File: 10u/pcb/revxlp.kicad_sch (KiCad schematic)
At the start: 126 parts, among them Q1 AO3416 N-channel MOSFET, SW1 SW_SPDT, SW2 SW_Push, U1 74HC595, U2 SeeeduinoXIAO_BLE

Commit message: feat: Optional backlighting for the bottom side.
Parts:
- added D_U0, D_U1, D_U10, D_U11, D_U2, D_U3, D_U4, D_U5, D_U6, D_U7, D_U8, D_U9: LED, Diode_SMD:D_1206_3216Metric_Pad1.42x1.75mm_HandSolder, symbol Device:LED
- added JP2: SolderJumper_2_Open, Jumper:SolderJumper-2_P1.3mm_Open_RoundedPad1.0x1.5mm, symbol Jumper:SolderJumper_2_Open
- added JP3: SolderJumper_2_Bridged, Jumper:SolderJumper-2_P1.3mm_Bridged_RoundedPad1.0x1.5mm, symbol Jumper:SolderJumper_2_Bridged
- added R_U0, R_U1, R_U10, R_U11, R_U2, R_U3, R_U4, R_U5, R_U6, R_U7, R_U8, R_U9: R, Resistor_SMD:R_1206_3216Metric_Pad1.30x1.75mm_HandSolder, symbol Device:R_Small_US
- JP1: footprint Jumper:SolderJumper-3_P1.3mm_Open_RoundedPad1.0x1.5mm -> Jumper:SolderJumper-3_P1.3mm_Bridged12_RoundedPad1.0x1.5mm; symbol 41_1350_pcb-rescue:SolderJumper_3_Open-Jumper -> Jumper:SolderJumper_3_Bridged12
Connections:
- net +3V3: now also JP1.3 (B); no longer JP1.1 (A)
- net +5V: now also D_U0.2 (A), D_U1.2 (A), D_U10.2 (A), D_U11.2 (A), D_U2.2 (A), D_U3.2 (A), D_U4.2 (A), D_U5.2 (A), D_U6.2 (A), D_U7.2 (A), D_U8.2 (A), D_U9.2 (A)
- net ledOut: now also JP3.1 (A); no longer Q1.3 (D)
- net at U2.14 (5V): now also JP1.1 (A); no longer JP1.3 (B)
- new net: JP2.2 (B), JP3.2 (B), Q1.3 (D)
- new net: D_U9.1 (K), R_U9.2
- new net: D_U11.1 (K), R_U11.2
- new net: D_U2.1 (K), R_U2.2
- new net: D_U3.1 (K), R_U3.2
- new net: D_U4.1 (K), R_U4.2
- new net: D_U10.1 (K), R_U10.2
- new net: D_U1.1 (K), R_U1.2
- new net: D_U8.1 (K), R_U8.2
- new net: D_U6.1 (K), R_U6.2
- new net: D_U5.1 (K), R_U5.2
- new net: D_U0.1 (K), R_U0.2
- new net: D_U7.1 (K), R_U7.2
- new net ledBottomOut: JP2.1 (A), R_U0.1, R_U1.1, R_U10.1, R_U11.1, R_U2.1, R_U3.1, R_U4.1, R_U5.1, R_U6.1, R_U7.1, R_U8.1, R_U9.1

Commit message: PCBA tweaks for 10u version.
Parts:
- BT2: MPN (none) -> SM02B-SRSS-TB(LF)(SN)
- D_A1: value D -> 1N4148W; MPN (none) -> 1N4148W
- D_A2, D_A3, D_A4, D_A5, D_B1, D_B2, D_B3, D_B4, D_B5, D_C1, D_C2, D_C3, D_C4, D_C5, D_D1, D_D2, D_D3, D_D4, D_D5, D_E1, D_E2, D_E3, D_E4, D_E5, D_F1, D_F2, D_F3, D_F4, D_F5, D_G0, D_G1, D_G2, D_G3, D_G4, D_G5: value D -> 1N4148W
- D_U0, D_U1: MPN (none) -> VLMB41P1Q2
- H1, H2, H3, H4, H5, H6, H7: MPN (none) -> SMTSO2020CTJ
- Q1: MPN (none) -> AO3416
- R_A1, R_A2, R_A3, R_A4, R_A5, R_AltG2, R_B1, R_B2, R_B3, R_B4, R_B5, R_C1, R_C2, R_C3, R_C4, R_C5, R_D1, R_D2, R_D3, R_D4, R_D5, R_E1, R_E2, R_E3, R_E4, R_E5, R_F1, R_F2, R_F3, R_F4, R_F5, R_G0, R_G1, R_G2, R_G3, R_G4, R_G5, R_U0, R_U1, R_U10, R_U11, R_U2, R_U3, R_U4, R_U5, R_U6, R_U7, R_U8, R_U9: value R -> 180
- SW1: MPN (none) -> PCM12
- SW2: MPN (none) -> EVQPUC02K
- SwA1, SwA2: MPN (none) -> CPG135001S30,VLMB41P1Q2
- U1: MPN (none) -> SN74HC595DR

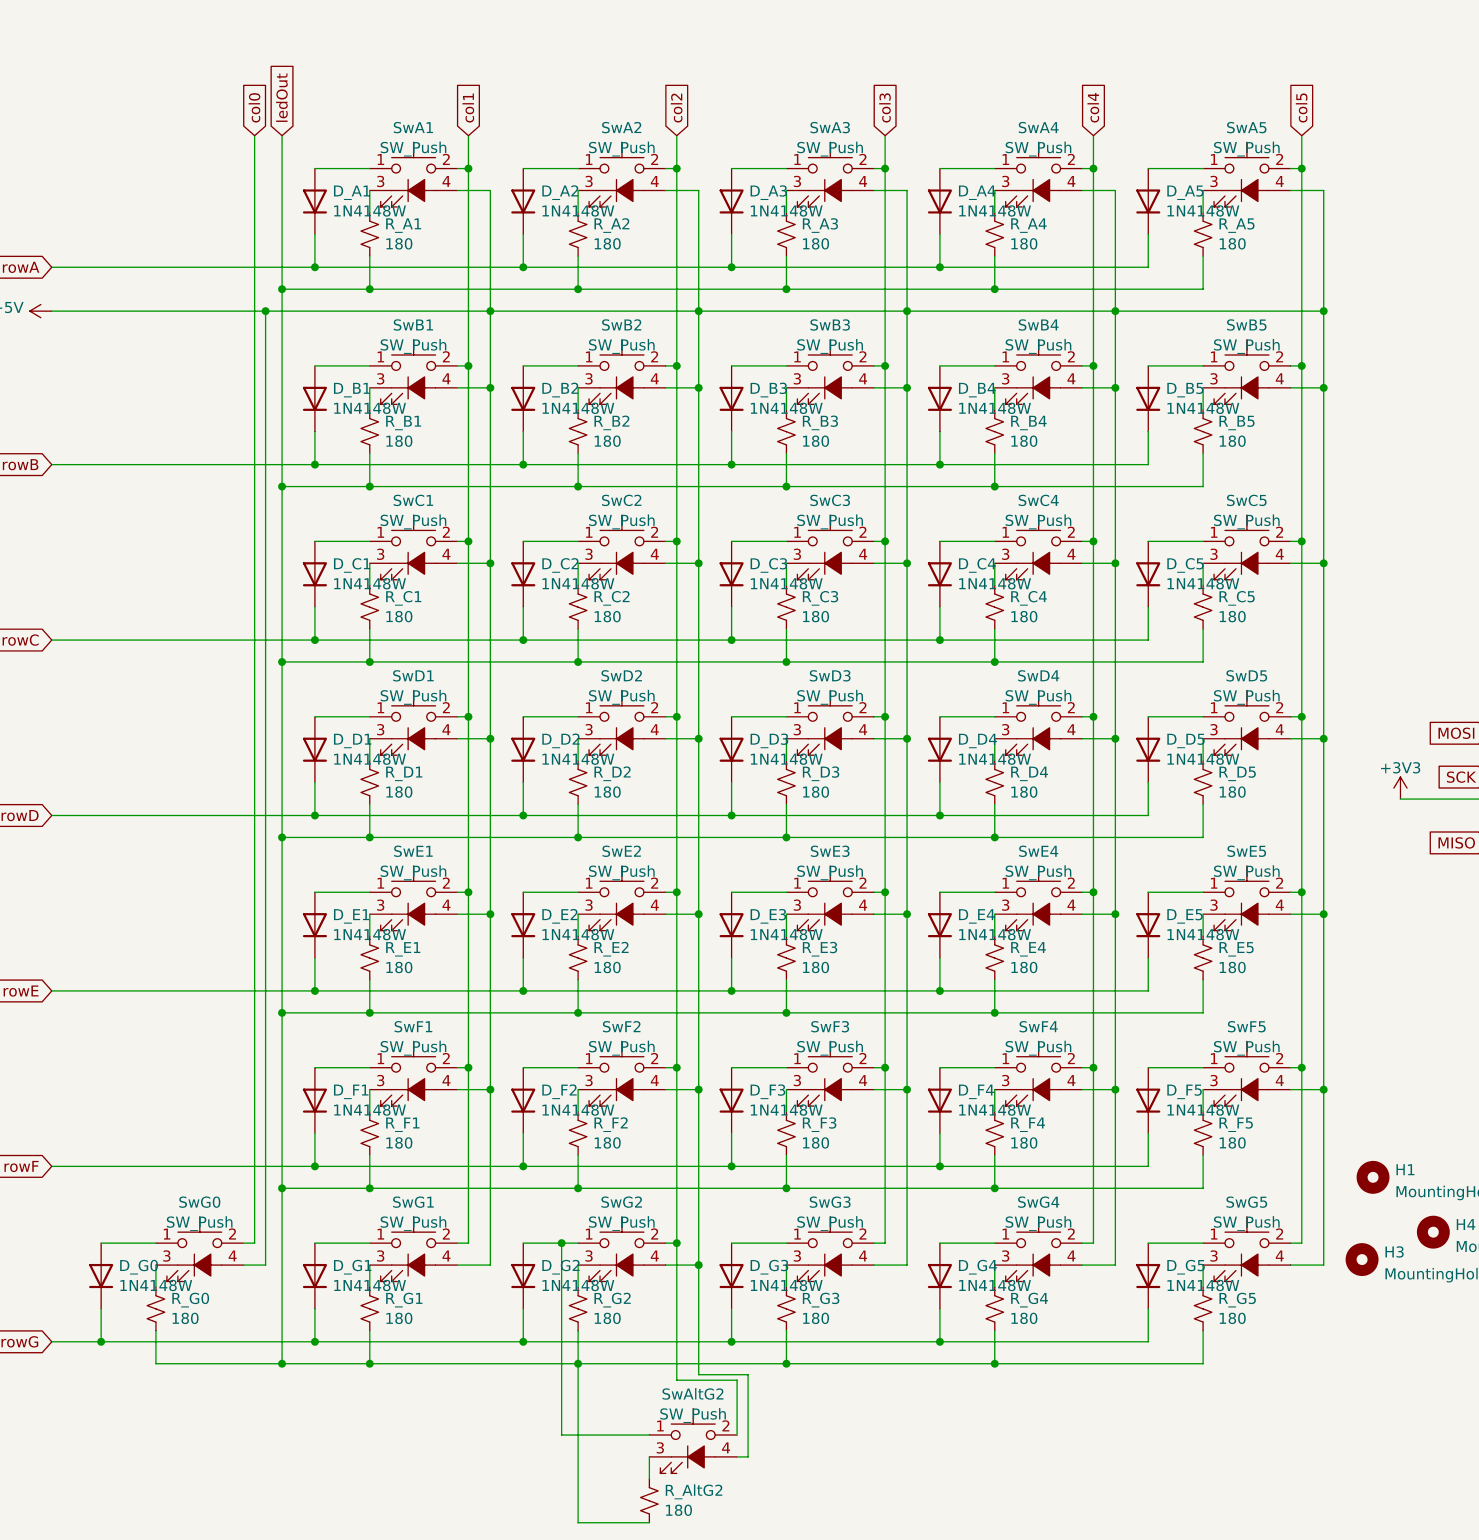
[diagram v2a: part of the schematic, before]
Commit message: Move to dedicated symbol and footprint for in-switch LEDs.
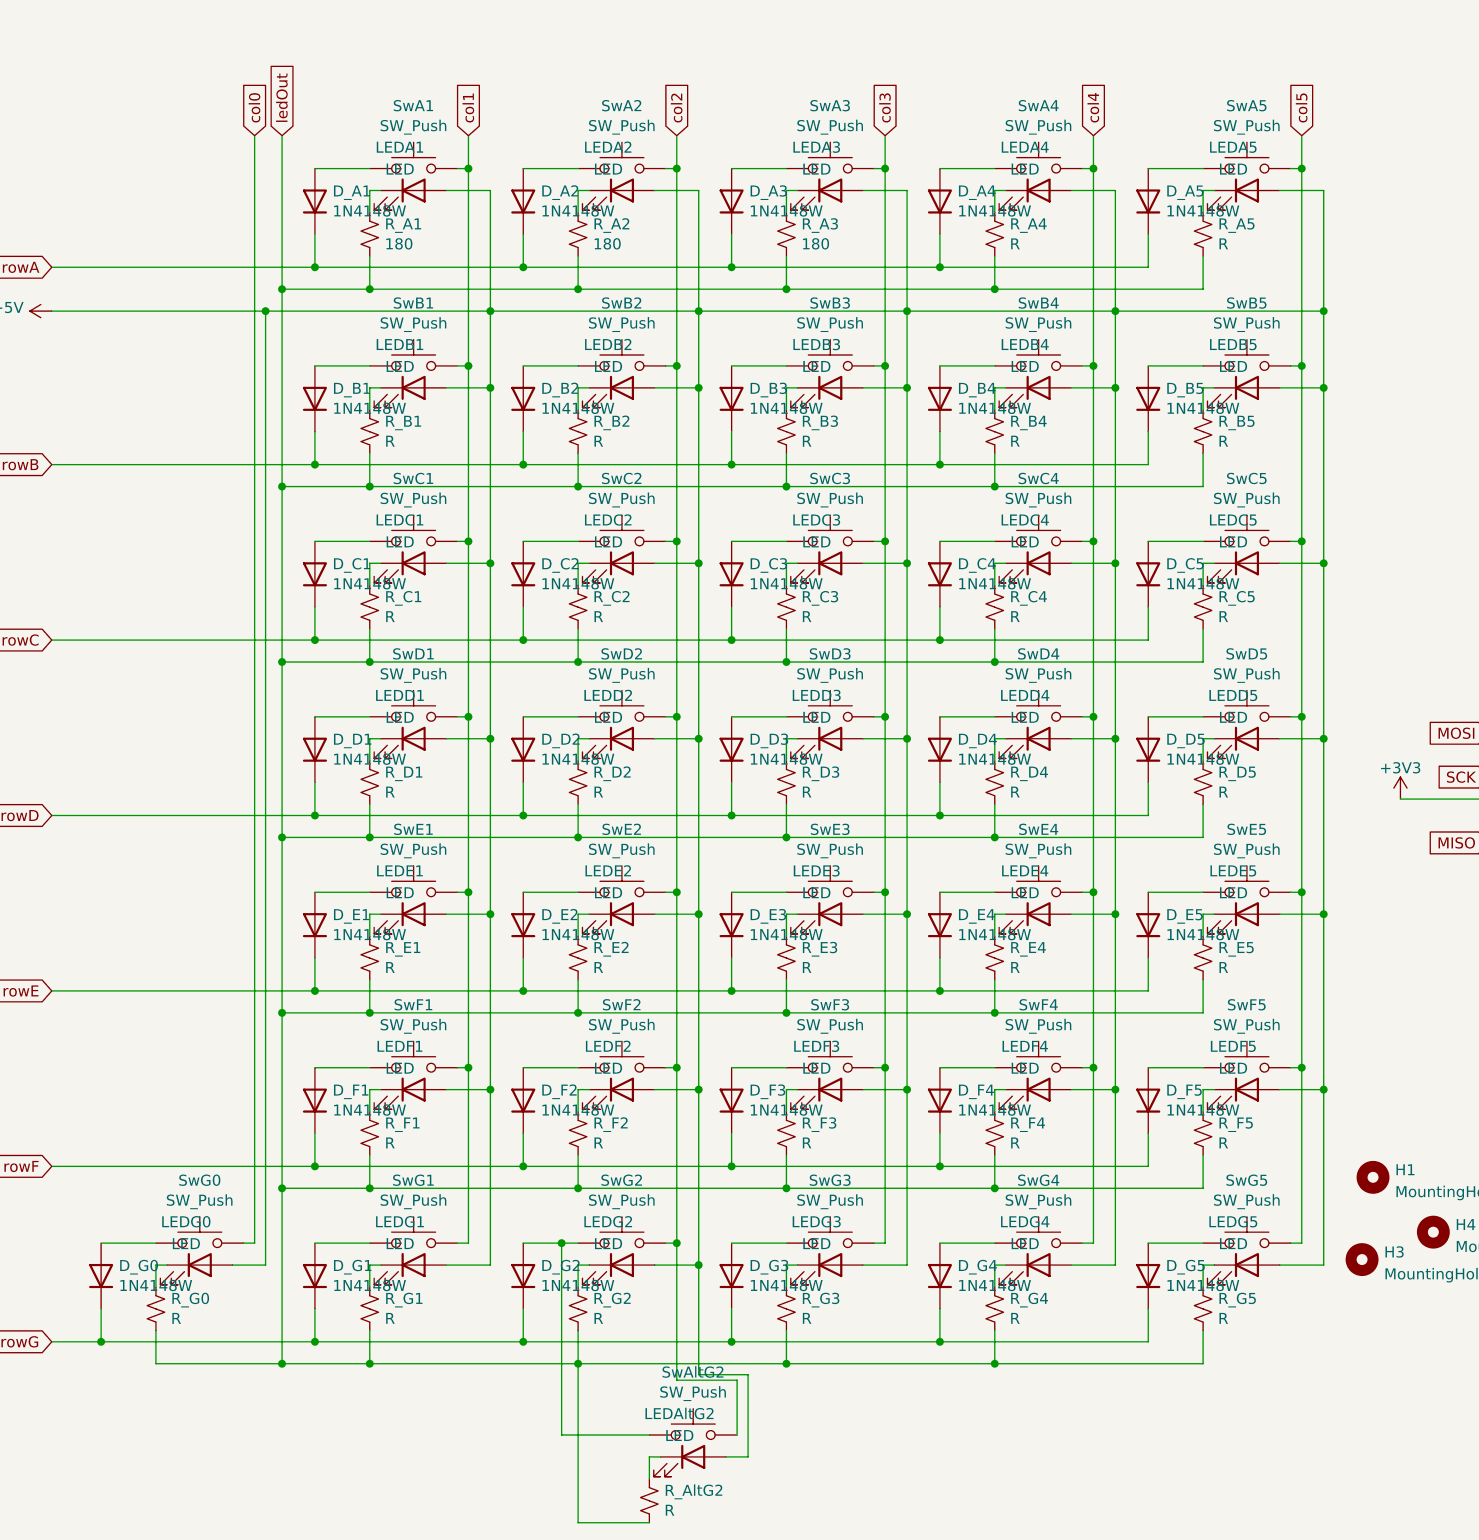
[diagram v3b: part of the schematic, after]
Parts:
- added LEDA1, LEDA2, LEDA3, LEDA4, LEDA5, LEDAltG2, LEDB1, LEDB2, LEDB3, LEDB4, LEDB5, LEDC1, LEDC2, LEDC3, LEDC4, LEDC5, LEDD1, LEDD2, LEDD3, LEDD4, LEDD5, LEDE1, LEDE2, LEDE3, LEDE4, LEDE5, LEDF1, LEDF2, LEDF3, LEDF4, LEDF5, LEDG0, LEDG1, LEDG2, LEDG3, LEDG4, LEDG5: LED, revxlp:PG1350_smdLed, symbol Device:LED
- R_A4, R_A5, R_AltG2, R_B1, R_B2, R_B3, R_B4, R_B5, R_C1, R_C2, R_C3, R_C4, R_C5, R_D1, R_D2, R_D3, R_D4, R_D5, R_E1, R_E2, R_E3, R_E4, R_E5, R_F1, R_F2, R_F3, R_F4, R_F5, R_G0, R_G1, R_G2, R_G3, R_G4, R_G5: value 180 -> R
- SwA1, SwA2: footprint revxlp:PG1350_socket_smdLed -> revxlp:PG1350_socket; symbol Switch:SW_Push_LED -> Switch:SW_Push; MPN CPG135001S30,VLMB41P1Q2 -> CPG135001S30
- SwA3, SwA4, SwA5, SwAltG2, SwB1, SwB2, SwB3, SwB4, SwB5, SwC1, SwC2, SwC3, SwC4, SwC5, SwD1, SwD2, SwD3, SwD4, SwD5, SwE1, SwE2, SwE3, SwE4, SwE5, SwF1, SwF2, SwF3, SwF4, SwF5, SwG0, SwG1, SwG2, SwG3, SwG4, SwG5: footprint revxlp:PG1350_socket_smdLed -> revxlp:PG1350_socket; symbol Switch:SW_Push_LED -> Switch:SW_Push; MPN (none) -> CPG135001S30
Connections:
- net +5V: now also LEDA1.2 (A), LEDA2.2 (A), LEDA3.2 (A), LEDA4.2 (A), LEDA5.2 (A), LEDAltG2.2 (A), LEDB1.2 (A), LEDB2.2 (A), LEDB3.2 (A), LEDB4.2 (A), LEDB5.2 (A), LEDC1.2 (A), LEDC2.2 (A), LEDC3.2 (A), LEDC4.2 (A), LEDC5.2 (A), LEDD1.2 (A), LEDD2.2 (A), LEDD3.2 (A), LEDD4.2 (A), LEDD5.2 (A), LEDE1.2 (A), LEDE2.2 (A), LEDE3.2 (A), LEDE4.2 (A), LEDE5.2 (A), LEDF1.2 (A), LEDF2.2 (A), LEDF3.2 (A), LEDF4.2 (A), LEDF5.2 (A), LEDG0.2 (A), LEDG1.2 (A), LEDG2.2 (A), LEDG3.2 (A), LEDG4.2 (A), LEDG5.2 (A); no longer SwA1.4 (A), SwA2.4 (A), SwA3.4 (A), SwA4.4 (A), SwA5.4 (A), SwAltG2.4 (A), SwB1.4 (A), SwB2.4 (A), SwB3.4 (A), SwB4.4 (A), SwB5.4 (A), SwC1.4 (A), SwC2.4 (A), SwC3.4 (A), SwC4.4 (A), SwC5.4 (A), SwD1.4 (A), SwD2.4 (A), SwD3.4 (A), SwD4.4 (A), SwD5.4 (A), SwE1.4 (A), SwE2.4 (A), SwE3.4 (A), SwE4.4 (A), SwE5.4 (A), SwF1.4 (A), SwF2.4 (A), SwF3.4 (A), SwF4.4 (A), SwF5.4 (A), SwG0.4 (A), SwG1.4 (A), SwG2.4 (A), SwG3.4 (A), SwG4.4 (A), SwG5.4 (A)
- net at R_A1.2: now also LEDA1.1 (K); no longer SwA1.3 (K)
- net at R_B1.2: now also LEDB1.1 (K); no longer SwB1.3 (K)
- net at R_C1.2: now also LEDC1.1 (K); no longer SwC1.3 (K)
- net at R_D1.2: now also LEDD1.1 (K); no longer SwD1.3 (K)
- net at R_E1.2: now also LEDE1.1 (K); no longer SwE1.3 (K)
- net at R_F1.2: now also LEDF1.1 (K); no longer SwF1.3 (K)
- net at R_G3.2: now also LEDG3.1 (K); no longer SwG3.3 (K)
- net at R_G4.2: now also LEDG4.1 (K); no longer SwG4.3 (K)
- net at R_A2.2: now also LEDA2.1 (K); no longer SwA2.3 (K)
- net at R_B2.2: now also LEDB2.1 (K); no longer SwB2.3 (K)
- net at R_C2.2: now also LEDC2.1 (K); no longer SwC2.3 (K)
- net at R_D2.2: now also LEDD2.1 (K); no longer SwD2.3 (K)
- net at R_E2.2: now also LEDE2.1 (K); no longer SwE2.3 (K)
- net at R_F2.2: now also LEDF2.1 (K); no longer SwF2.3 (K)
- net at R_A3.2: now also LEDA3.1 (K); no longer SwA3.3 (K)
- net at R_B3.2: now also LEDB3.1 (K); no longer SwB3.3 (K)
- net at R_C3.2: now also LEDC3.1 (K); no longer SwC3.3 (K)
- net at R_D3.2: now also LEDD3.1 (K); no longer SwD3.3 (K)
- net at R_E3.2: now also LEDE3.1 (K); no longer SwE3.3 (K)
- net at R_F3.2: now also LEDF3.1 (K); no longer SwF3.3 (K)
- net at R_A4.2: now also LEDA4.1 (K); no longer SwA4.3 (K)
- net at R_B4.2: now also LEDB4.1 (K); no longer SwB4.3 (K)
- net at R_C4.2: now also LEDC4.1 (K); no longer SwC4.3 (K)
- net at R_D4.2: now also LEDD4.1 (K); no longer SwD4.3 (K)
- net at R_E4.2: now also LEDE4.1 (K); no longer SwE4.3 (K)
- net at R_F4.2: now also LEDF4.1 (K); no longer SwF4.3 (K)
- net at R_A5.2: now also LEDA5.1 (K); no longer SwA5.3 (K)
- net at R_B5.2: now also LEDB5.1 (K); no longer SwB5.3 (K)
- net at R_C5.2: now also LEDC5.1 (K); no longer SwC5.3 (K)
- net at R_D5.2: now also LEDD5.1 (K); no longer SwD5.3 (K)
- net at R_E5.2: now also LEDE5.1 (K); no longer SwE5.3 (K)
- net at R_F5.2: now also LEDF5.1 (K); no longer SwF5.3 (K)
- net at R_G1.2: now also LEDG1.1 (K); no longer SwG1.3 (K)
- net at R_G2.2: now also LEDG2.1 (K); no longer SwG2.3 (K)
- net at R_G5.2: now also LEDG5.1 (K); no longer SwG5.3 (K)
- net at R_G0.2: now also LEDG0.1 (K); no longer SwG0.3 (K)
- net at R_AltG2.2: now also LEDAltG2.1 (K); no longer SwAltG2.3 (K)

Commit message: Silk cleanup.
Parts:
- JP2: value SolderJumper_2_Open -> Bottom
- JP3: value SolderJumper_2_Bridged -> Per-Key
